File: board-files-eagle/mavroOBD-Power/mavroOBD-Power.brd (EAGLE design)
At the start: 41 x 20 mm, 12 parts, among them U2 TPS793xx

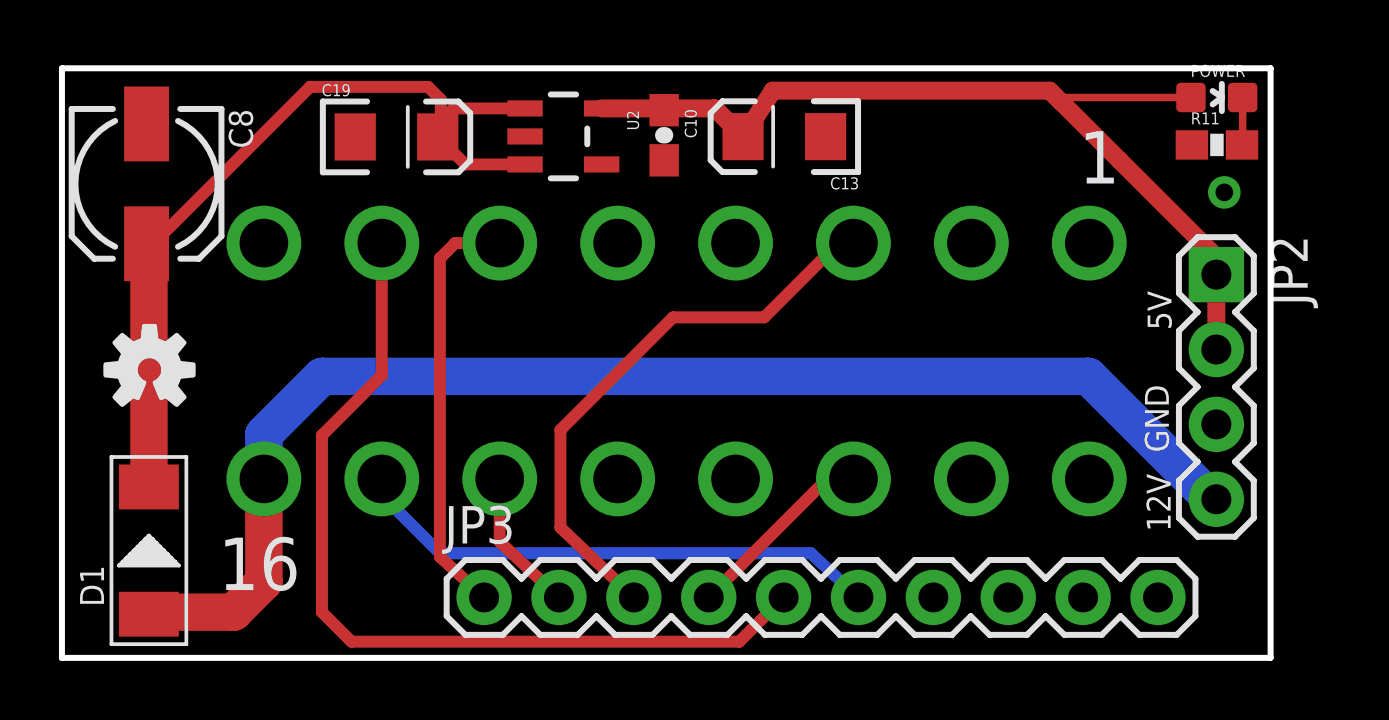
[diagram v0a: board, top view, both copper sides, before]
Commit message: Fixed incorrect pin assignment
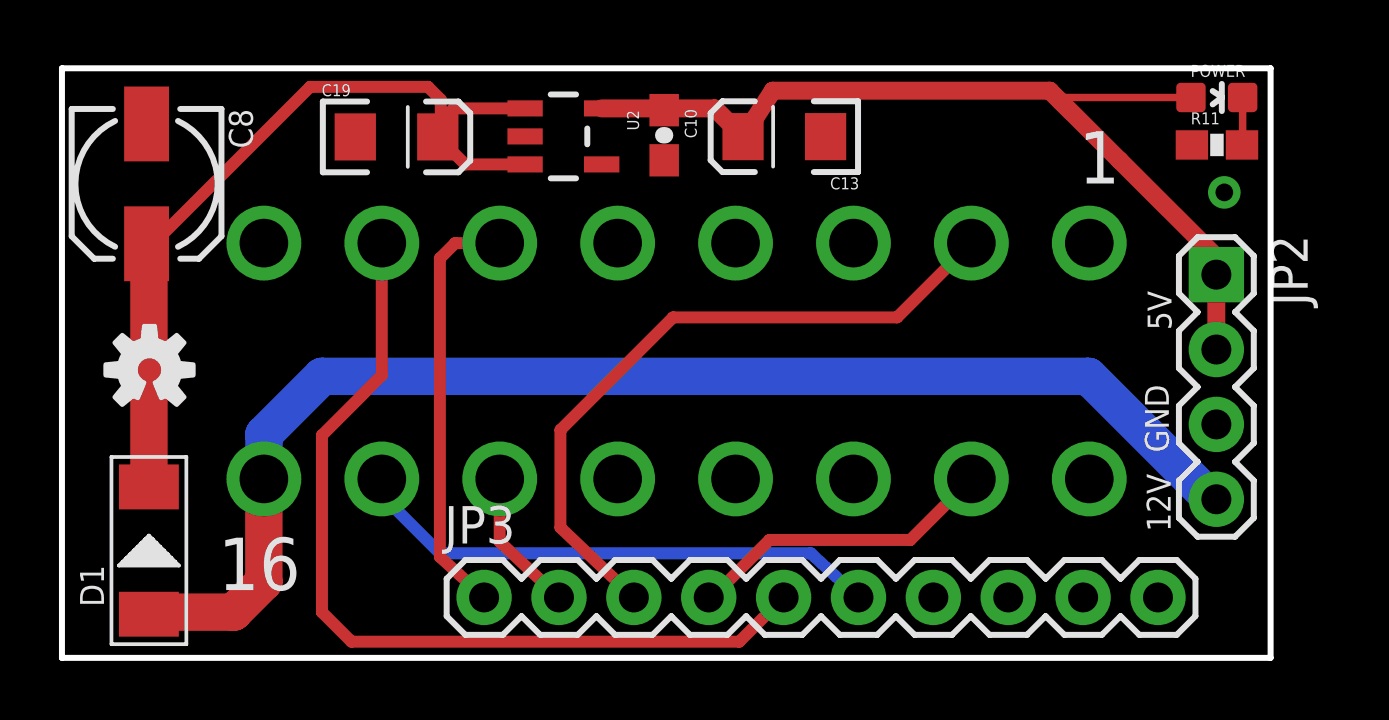
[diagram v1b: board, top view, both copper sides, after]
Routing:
- net CAN_P10: track 6.58 -> 10.7 mm
- net CAN_P2: track 19.3 -> 23.3 mm
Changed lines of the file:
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@@
 <layer number="112" name="tSilk" color="7" fill="1" visible="no" active="no"/>
 <layer number="113" name="IDFDebug" color="7" fill="1" visible="no" active="yes"/>
+<layer number="114" name="Badge_Outline" color="7" fill="1" visible="yes" active="yes"/>
+<layer number="115" name="ReferenceISLANDS" color="7" fill="1" visible="yes" active="yes"/>
 <layer number="116" name="Patch_BOT" color="9" fill="4" visible="no" active="yes"/>
 <layer number="118" name="Rect_Pads" color="7" fill="1" visible="no" active="no"/>
@@
 <contactref element="U$1" pad="2"/>
 <contactref element="JP3" pad="3"/>
-<wire x1="26.85" y1="14.07" x2="26.34" y2="14.07" width="0.4064" layer="1"/>
-<wire x1="26.34" y1="14.07" x2="23.82" y2="11.55" width="0.4064" layer="1"/>
-<wire x1="23.82" y1="11.55" x2="20.73" y2="11.55" width="0.4064" layer="1"/>
 <wire x1="20.73" y1="11.55" x2="16.91" y2="7.73" width="0.4064" layer="1"/>
 <wire x1="16.91" y1="7.73" x2="16.91" y2="4.42" width="0.4064" layer="1"/>
 <wire x1="16.91" y1="4.42" x2="19.4" y2="2.05" width="0.4064" layer="1"/>
+<wire x1="20.73" y1="11.55" x2="28.33" y2="11.55" width="0.4064" layer="1"/>
+<wire x1="28.33" y1="11.55" x2="30.85" y2="14.07" width="0.4064" layer="1"/>
 </signal>
 <signal name="CAN_P10">
 <contactref element="U$1" pad="10"/>
 <contactref element="JP3" pad="4"/>
-<wire x1="26.85" y1="6.07" x2="25.96" y2="6.07" width="0.4064" layer="1"/>
-<wire x1="25.96" y1="6.07" x2="21.94" y2="2.05" width="0.4064" layer="1"/>
+<wire x1="21.94" y1="2.05" x2="21.94" y2="1.94" width="0.4064" layer="1"/>
+<wire x1="21.94" y1="1.94" x2="24" y2="4" width="0.4064" layer="1"/>
+<wire x1="24" y1="4" x2="28.78" y2="4" width="0.4064" layer="1"/>
+<wire x1="28.78" y1="4" x2="30.85" y2="6.07" width="0.4064" layer="1"/>
 </signal>
 <signal name="CAN_P7">
